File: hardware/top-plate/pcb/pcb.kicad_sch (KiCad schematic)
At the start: 48 parts, among them SW1 MT-0-102-A101-M200-RS+PJ, U1 RP2040-ZERO

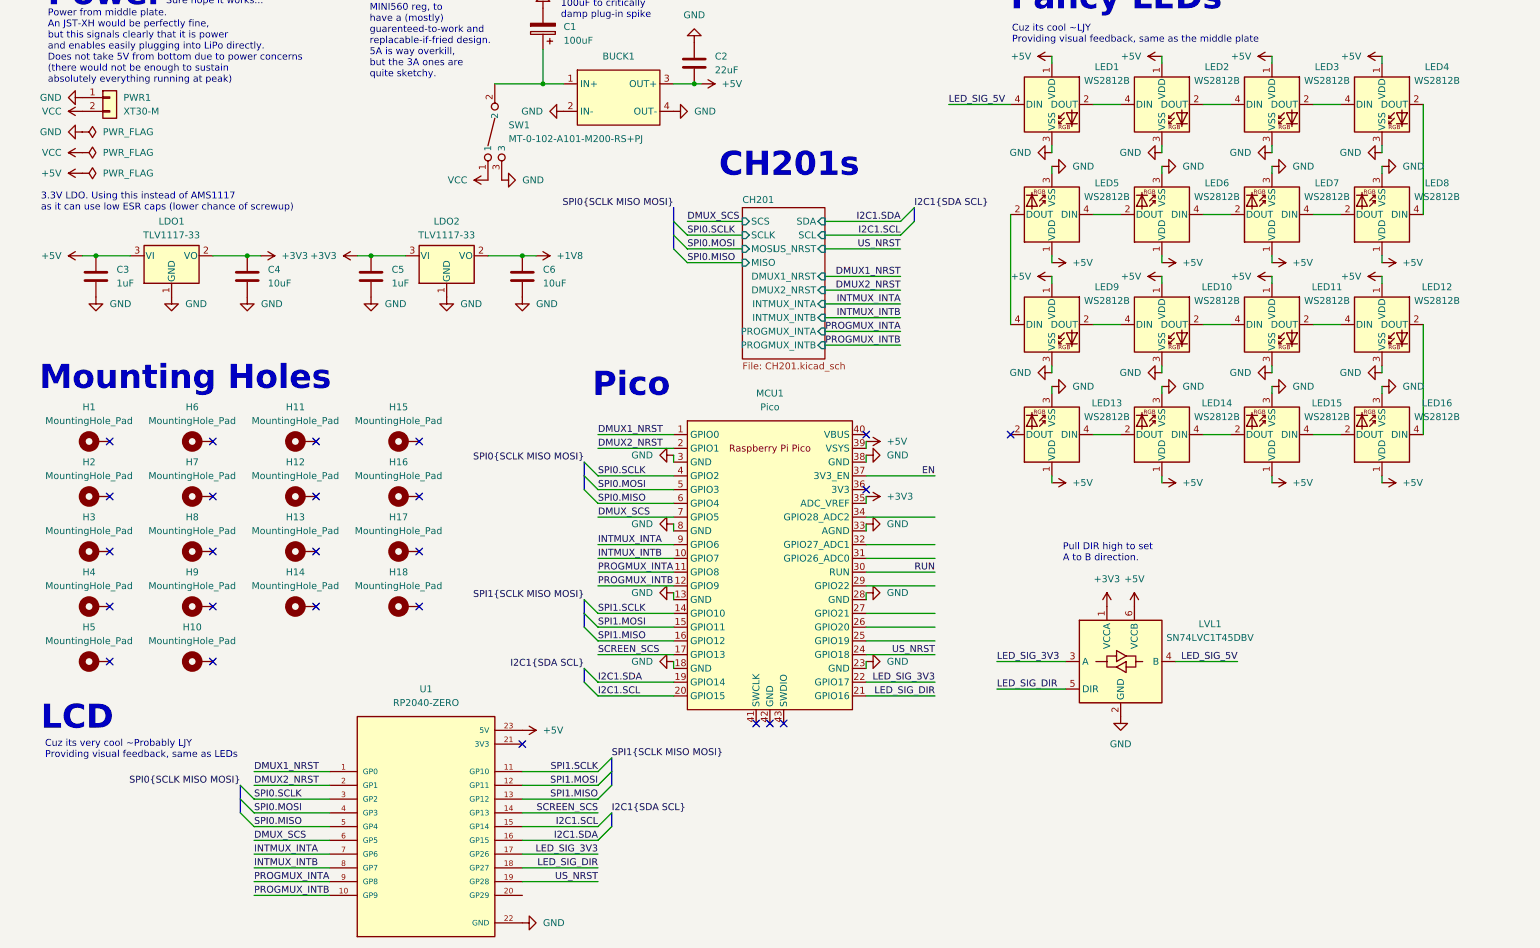
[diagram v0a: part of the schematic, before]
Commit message: fixed up symbols for oled and ultrasound
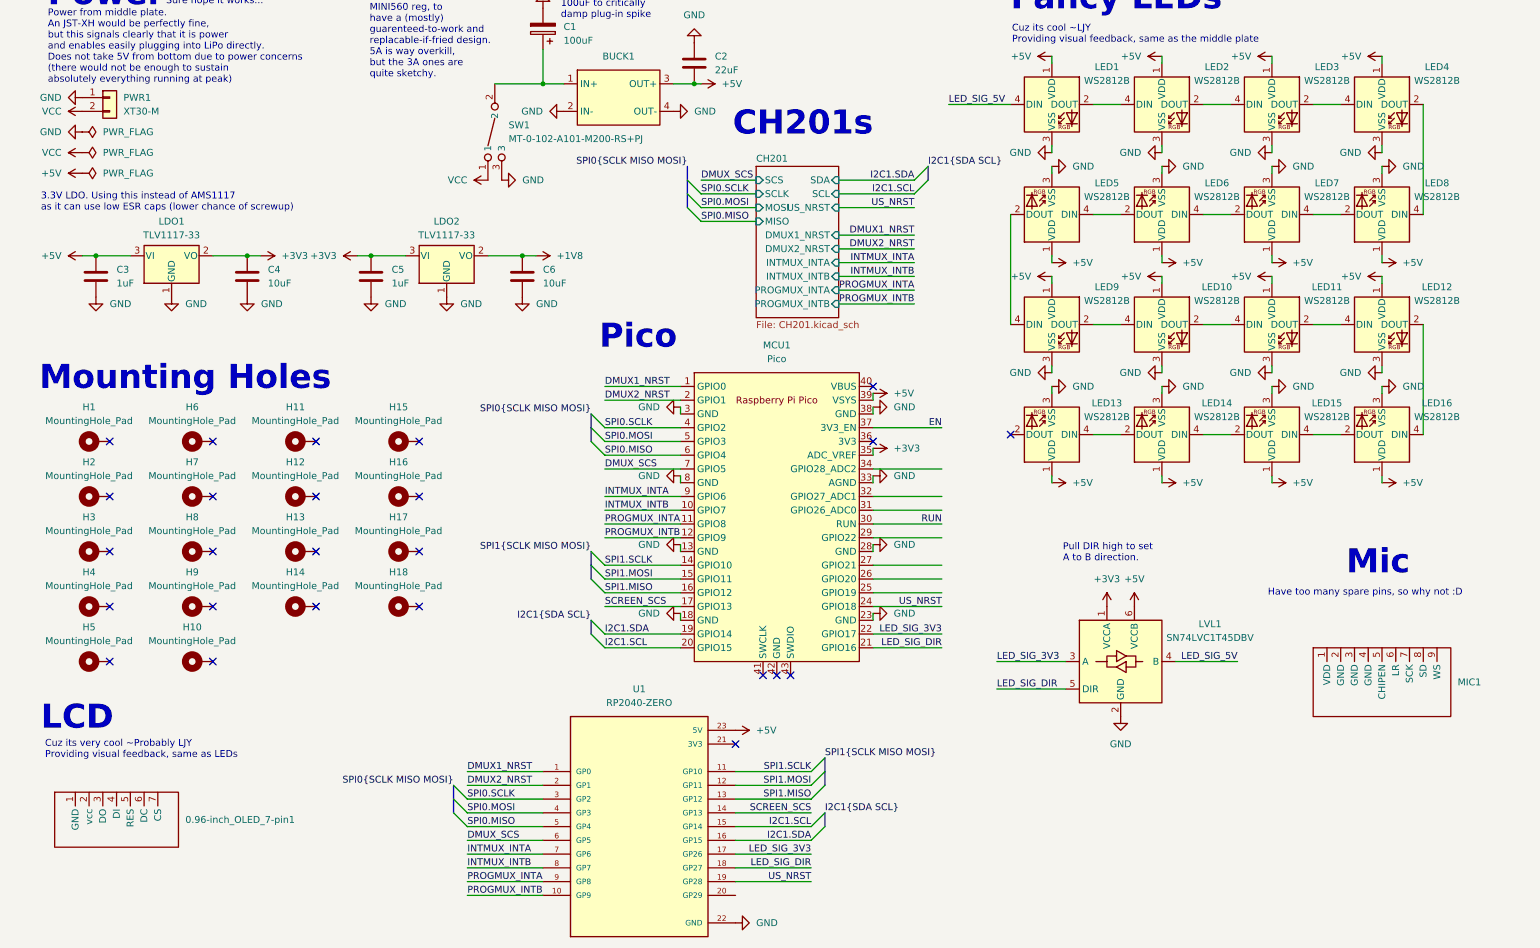
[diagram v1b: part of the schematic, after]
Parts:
- added 0.96-inch_OLED_7-pin1: ~, symbol 0.96-inch OLED 7-pin:0.96-inch_OLED_7-pin
- added MIC1: ~, symbol INMP44:INMP441
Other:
- note added: "Have too many spare pins, so why not :D"
- note added: "Mic"
- moved on the sheet: MCU1, U1

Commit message: fixed up symbols and footprints for top plate, and completed top plate schematic (other than modifications for better routing)
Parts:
- removed 0.96-inch_OLED_7-pin1: ~, symbol 0.96-inch OLED 7-pin:0.96-inch_OLED_7-pin
- removed U1: RP2040-ZERO, Snapeda:RP2040-ZERO_MODULE_RP2040-ZERO, symbol Snapeda:RP2040-ZERO
- added IMU1, IMU2: ~, symbol GY-ICM20948V2:GY-ICM20948V2
- added J1: Conn_01x02, 4ms_Connector:Pins_1x02_2.54mm_TH, symbol PCM_4ms_Connector:Conn_01x02
- added OLED1: ~, 0.96-inch_OLED_7-pin:0.96-inch_OLED_7-pin, symbol 0.96-inch OLED 7-pin:0.96-inch_OLED_7-pin
- added R4, R5: 2.2kR, PCM_Resistor_SMD_AKL:R_1206_3216Metric_Pad1.30x1.75mm_HandSolder, symbol Device:R
- added R6: 10kR, PCM_Resistor_SMD_AKL:R_1206_3216Metric_Pad1.30x1.75mm_HandSolder, symbol Device:R
- MCU1: footprint RP-Pico Libraries:RPi_Pico_SMD_TH_USBC_cable_cutout -> RP-Pico Libraries:RPi_Pico_SMD_TH
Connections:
- net SCREEN_SCS is gone; now on net PROGMUX_INTA: MCU1.17 (GPIO13)
- net SPI1.MISO is gone; now on net US_NRST: MCU1.16 (GPIO12)
- net +3V3: now also MIC1.2 (VDD), IMU1.1 (VCC), IMU2.1 (VCC), OLED1.2 (VCC), R4.1, R5.1, R6.1
- net EN: now also J1.1 (Pin_1)
- net GND: now also MIC1.1 (GND), IMU1.10 (FSYNC), IMU1.2 (GND), IMU2.10 (FSYNC), IMU2.2 (GND), OLED1.1 (GND)
- net I2C1.SCL: now also R5.2
- net I2C1.SDA: now also R4.2
- net INTMUX_INTA: now also MCU1.34 (GPIO28_ADC2); no longer MCU1.9 (GPIO6)
- net PROGMUX_INTA: no longer MCU1.11 (GPIO8)
- net RUN: now also J1.2 (Pin_2)
- net SPI0.MISO: now also IMU1.7 (AD0/SDO), IMU2.7 (AD0/SDO)
- net SPI0.MOSI: now also IMU1.4 (SDA/SDI), IMU2.4 (SDA/SDI)
- net SPI0.SCLK: now also IMU1.3 (SCL/SCLK), IMU2.3 (SCL/SCLK)
- net SPI1.MOSI: now also OLED1.4 (D1/SDI)
- net SPI1.SCLK: now also OLED1.3 (D0/SCLK)
- net US_NRST: now also R6.2; no longer MCU1.24 (GPIO18)
- net MIC1.SD: now reaches MIC1.3 (SD)
- net MIC1.SD: now also MCU1.27 (GPIO21)
- net MIC1.L/R: now reaches MIC1.4 (L/R)
- net MIC1.L/R: now also MCU1.26 (GPIO20)
- net MIC1.WS: now reaches MIC1.5 (WS)
- net MIC1.WS: now also MCU1.25 (GPIO19)
- net MIC1.SCK: now reaches MIC1.6 (SCK)
- net MIC1.SCK: now also MCU1.24 (GPIO18)
- net OLED.SCS: now reaches MCU1.29 (GPIO22)
- net OLED.SCS: now also OLED1.7 (CS)
- net OLED.D/C#: now reaches MCU1.31 (GPIO26_ADC0)
- net OLED.D/C#: now also OLED1.6 (D/C#)
- net OLED.NRST: now reaches MCU1.32 (GPIO27_ADC1)
- net OLED.NRST: now also OLED1.5 (NRST)
- net INTMUX_INTB renamed IMU1.NCS
- net IMU1.NCS: now also IMU1.9 (NCS)
- net PROGMUX_INTB renamed IMU2.NCS
- net IMU2.NCS: now also IMU2.9 (NCS)
- new net IMU1.INT: IMU1.8 (INT), MCU1.9 (GPIO6)
- new net IMU2.INT: IMU2.8 (INT), MCU1.11 (GPIO8)
- no-connect marks 25 -> 34
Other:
- note added: "Datasheet says to connect to GND if not using FSYNC."
- note added: "IMUs"
- note added: "No other devices uses PWM, and every pin has it, so it probably can work. I2S input can be done through PIO as well. Not super important to guarentee working."
- moved on the sheet: BUCK1, C1, C2, C3, C4, C5, C6, H1, H10, H11, H12, H13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
